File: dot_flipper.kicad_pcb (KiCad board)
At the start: 2 copper layers, 71 x 10 mm, 3 parts, among them U1 7_flip_dots

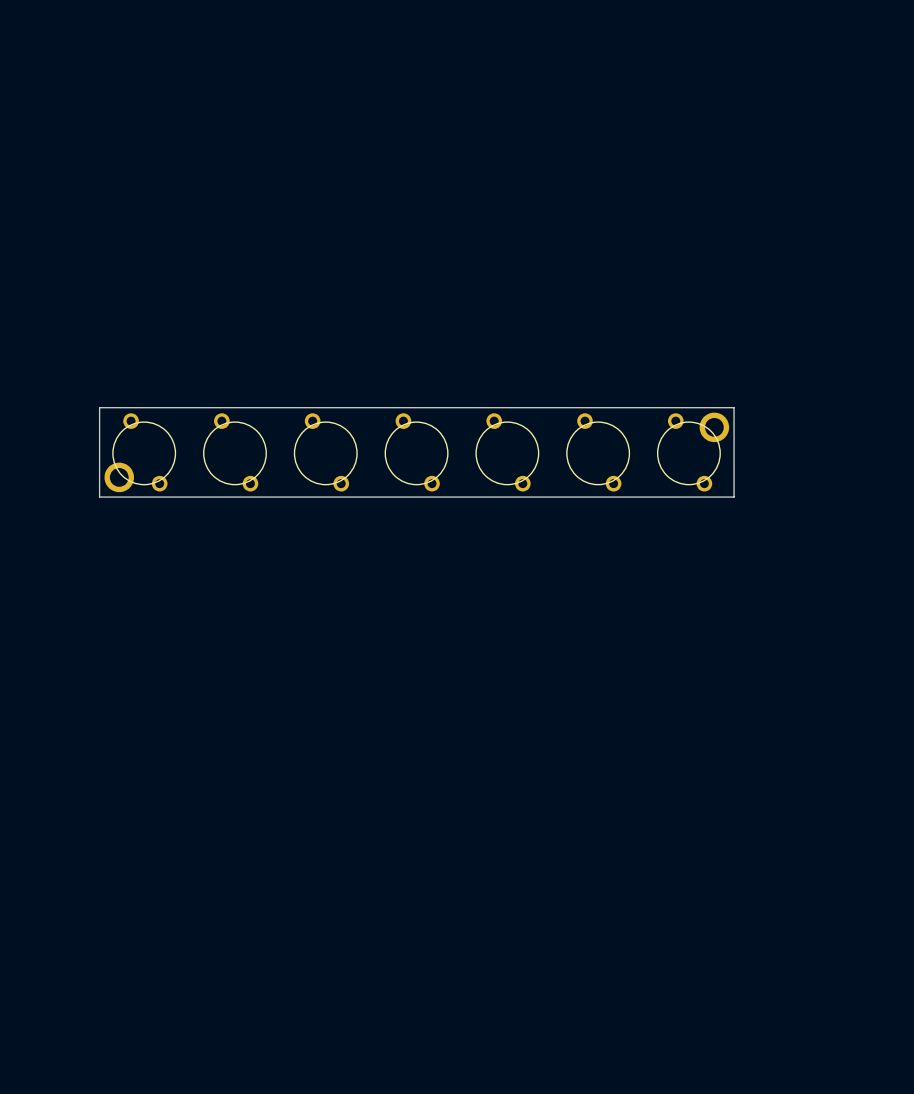
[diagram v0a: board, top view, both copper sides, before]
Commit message: Rough component placement
Slightly tweaked flipdot footprint to match my measurements and datasheet better
Created board outline, interfaces.
Rough component placement.
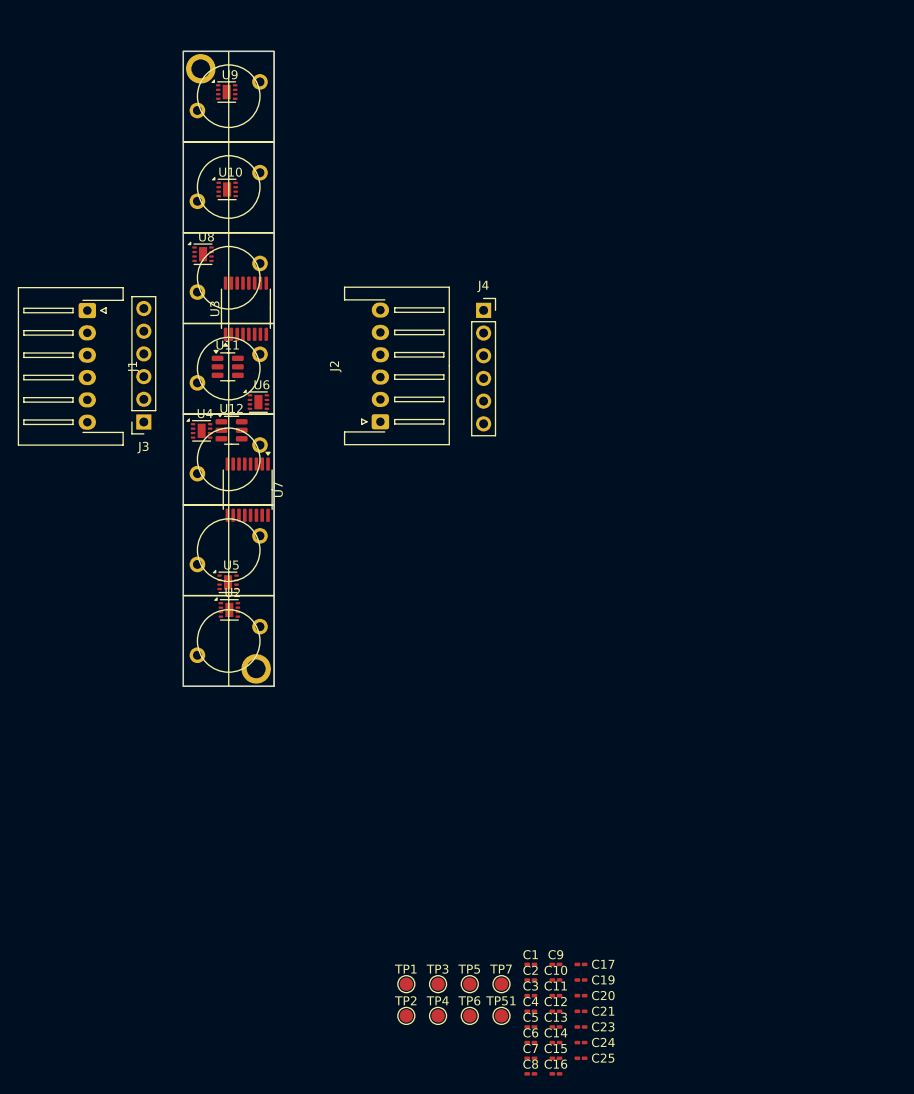
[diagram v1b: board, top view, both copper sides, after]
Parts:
- added C1: 100n/16V, Capacitor_SMD:C_0201_0603Metric_Pad0.64x0.40mm_HandSolder, F.Cu at (80.8, 122.1)
- added C10: 100n/16V, Capacitor_SMD:C_0201_0603Metric_Pad0.64x0.40mm_HandSolder, F.Cu at (83.7, 123.8)
- added C11: 100n/16V, Capacitor_SMD:C_0201_0603Metric_Pad0.64x0.40mm_HandSolder, F.Cu at (83.7, 125.6)
- added C12: 10uF/16V, Capacitor_SMD:C_0201_0603Metric_Pad0.64x0.40mm_HandSolder, F.Cu at (83.7, 127.3)
- added C13: 10uF/16V, Capacitor_SMD:C_0201_0603Metric_Pad0.64x0.40mm_HandSolder, F.Cu at (83.7, 129.1)
- added C14: 100n, Capacitor_SMD:C_0201_0603Metric_Pad0.64x0.40mm_HandSolder, F.Cu at (83.7, 130.8)
- added C15: 100n/16V, Capacitor_SMD:C_0201_0603Metric_Pad0.64x0.40mm_HandSolder, F.Cu at (83.7, 132.6)
- added C16: 100n/16V, Capacitor_SMD:C_0201_0603Metric_Pad0.64x0.40mm_HandSolder, F.Cu at (83.7, 134.3)
- added C17: 100n/16V, Capacitor_SMD:C_0201_0603Metric_Pad0.64x0.40mm_HandSolder, F.Cu at (86.5, 122.1)
- added C19: 100n/16V, Capacitor_SMD:C_0201_0603Metric_Pad0.64x0.40mm_HandSolder, F.Cu at (86.5, 123.8)
- added C2: 100n/16V, Capacitor_SMD:C_0201_0603Metric_Pad0.64x0.40mm_HandSolder, F.Cu at (80.8, 123.8)
- added C20: 100n/16V, Capacitor_SMD:C_0201_0603Metric_Pad0.64x0.40mm_HandSolder, F.Cu at (86.5, 125.6)
- added C21: 100n/16V, Capacitor_SMD:C_0201_0603Metric_Pad0.64x0.40mm_HandSolder, F.Cu at (86.5, 127.3)
- added C23: 10uF/16V, Capacitor_SMD:C_0201_0603Metric_Pad0.64x0.40mm_HandSolder, F.Cu at (86.5, 129.1)
- added C24: 10uF/16V, Capacitor_SMD:C_0201_0603Metric_Pad0.64x0.40mm_HandSolder, F.Cu at (86.5, 130.8)
- added C25: 10uF/16V, Capacitor_SMD:C_0201_0603Metric_Pad0.64x0.40mm_HandSolder, F.Cu at (86.5, 132.6)
- added C3: 100n, Capacitor_SMD:C_0201_0603Metric_Pad0.64x0.40mm_HandSolder, F.Cu at (80.8, 125.6)
- added C4: 10uF/16V, Capacitor_SMD:C_0201_0603Metric_Pad0.64x0.40mm_HandSolder, F.Cu at (80.8, 127.3)
- added C5: 100n/16V, Capacitor_SMD:C_0201_0603Metric_Pad0.64x0.40mm_HandSolder, F.Cu at (80.8, 129.1)
- added C6: 100n/16V, Capacitor_SMD:C_0201_0603Metric_Pad0.64x0.40mm_HandSolder, F.Cu at (80.8, 130.8)
- added C7: 10uF/16V, Capacitor_SMD:C_0201_0603Metric_Pad0.64x0.40mm_HandSolder, F.Cu at (80.8, 132.6)
- added C8: 100n/16V, Capacitor_SMD:C_0201_0603Metric_Pad0.64x0.40mm_HandSolder, F.Cu at (80.8, 134.3)
- added C9: 100n/16V, Capacitor_SMD:C_0201_0603Metric_Pad0.64x0.40mm_HandSolder, F.Cu at (83.7, 122.1)
- added J1: Conn_01x06_Socket, Connector_JST:JST_XH_S6B-XH-A-1_1x06_P2.50mm_Horizontal, F.Cu at (31.2, 48.9)
- added J2: Conn_01x06_Socket, Connector_JST:JST_XH_S6B-XH-A-1_1x06_P2.50mm_Horizontal, F.Cu at (64.0, 61.3)
- added J3: Conn_01x06_Socket, Connector_PinSocket_2.54mm:PinSocket_1x06_P2.54mm_Vertical, F.Cu at (37.5, 61.4)
- added J4: Conn_01x06_Socket, Connector_PinSocket_2.54mm:PinSocket_1x06_P2.54mm_Vertical, F.Cu at (75.6, 48.9)
- added TP1: SEROUT1, TestPoint:TestPoint_Pad_D1.5mm, F.Cu at (66.9, 124.3)
- added TP2: SLEEP, TestPoint:TestPoint_Pad_D1.5mm, F.Cu at (66.9, 127.8)
- added TP3: LATCH, TestPoint:TestPoint_Pad_D1.5mm, F.Cu at (70.5, 124.3)
- added TP4: SRCLK, TestPoint:TestPoint_Pad_D1.5mm, F.Cu at (70.5, 127.8)
- added TP5: SERIN, TestPoint:TestPoint_Pad_D1.5mm, F.Cu at (74.0, 124.3)
- added TP51: SEROUT2, TestPoint:TestPoint_Pad_D1.5mm, F.Cu at (77.6, 127.8)
- added TP6: VCC, TestPoint:TestPoint_Pad_D1.5mm, F.Cu at (74.0, 127.8)
- added TP7: GND, TestPoint:TestPoint_Pad_D1.5mm, F.Cu at (77.6, 124.3)
- added U10: DRV8837C, Package_SON:WSON-8-1EP_2x2mm_P0.5mm_EP0.9x1.6mm, F.Cu at (46.9, 35.3)
- added U11: CDSOT236-T05C, Package_TO_SOT_SMD:SOT-23-6, F.Cu at (46.9, 55.2)
- added U12: CDSOT236-T05C, Package_TO_SOT_SMD:SOT-23-6, F.Cu at (47.4, 62.3)
- added U2: DRV8837C, Package_SON:WSON-8-1EP_2x2mm_P0.5mm_EP0.9x1.6mm, F.Cu at (47.1, 82.4)
- added U3: 74HC595, Package_SO:TSSOP-16_4.4x5mm_P0.65mm, F.Cu at (49.0, 48.7)
- added U4: DRV8837C, Package_SON:WSON-8-1EP_2x2mm_P0.5mm_EP0.9x1.6mm, F.Cu at (44.0, 62.4)
- added U5: DRV8837C, Package_SON:WSON-8-1EP_2x2mm_P0.5mm_EP0.9x1.6mm, F.Cu at (47.0, 79.3)
- added U6: DRV8837C, Package_SON:WSON-8-1EP_2x2mm_P0.5mm_EP0.9x1.6mm, F.Cu at (50.4, 59.1)
- added U7: 74HC595, Package_SO:TSSOP-16_4.4x5mm_P0.65mm, F.Cu at (49.2, 68.9)
- added U8: DRV8837C, Package_SON:WSON-8-1EP_2x2mm_P0.5mm_EP0.9x1.6mm, F.Cu at (44.2, 42.6)
- added U9: DRV8837C, Package_SON:WSON-8-1EP_2x2mm_P0.5mm_EP0.9x1.6mm, F.Cu at (46.8, 24.4)
- moved H2 70.1 mm to (43.9, 21.8)
- moved U1 27.2 mm to (43.5, 87.5), turned to 90 degrees
- moved H1 26.3 mm to (50.1, 89.0)
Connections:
- U1 pad 1-UA: unconnected-(U1A-a-Pad1-UA) -> Net-(U1A-a)
- U1 pad 1-UB: unconnected-(U1B-a-Pad1-UB) -> Net-(U1B-a)
- U1 pad 1-UC: unconnected-(U1C-a-Pad1-UC) -> Net-(U1C-a)
- U1 pad 1-UD: unconnected-(U1D-a-Pad1-UD) -> Net-(U1D-a)
- U1 pad 1-UE: unconnected-(U1E-a-Pad1-UE) -> Net-(U1E-a)
- U1 pad 1-UF: unconnected-(U1F-a-Pad1-UF) -> Net-(U10-OUT2)
- U1 pad 1-UG: unconnected-(U1G-a-Pad1-UG) -> Net-(U1G-a)
- U1 pad 2-UA: unconnected-(U1A-b-Pad2-UA) -> Net-(U1A-b)
- U1 pad 2-UB: unconnected-(U1B-b-Pad2-UB) -> Net-(U1B-b)
- U1 pad 2-UC: unconnected-(U1C-b-Pad2-UC) -> Net-(U1C-b)
- U1 pad 2-UD: unconnected-(U1D-b-Pad2-UD) -> Net-(U1D-b)
- U1 pad 2-UE: unconnected-(U1E-b-Pad2-UE) -> Net-(U1E-b)
- U1 pad 2-UF: unconnected-(U1F-b-Pad2-UF) -> Net-(U10-OUT1)
- U1 pad 2-UG: unconnected-(U1G-b-Pad2-UG) -> Net-(U1G-b)
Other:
- board size 71 x 10 mm -> 10.2 x 71 mm
- board text removed: "+"
- board text removed: "-"
- board text removed: ".wordpress.com"
- board text removed: "12V"
- board text removed: "C"
- board text removed: "CLK"
- board text removed: "D"
- board text removed: "DATA"
- board text removed: "DOT FLIPPER v1.1"
- board text removed: "GND"
- board text removed: "INPUT"
- board text removed: "OPT1"
- board text removed: "OPT2"
- board text removed: "OUTPUT"
- board text removed: "P"
- board text removed: "PierreMuth"

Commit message: Power supply mod
Connected VM to VCC to simplify operation and make PCB layout easier
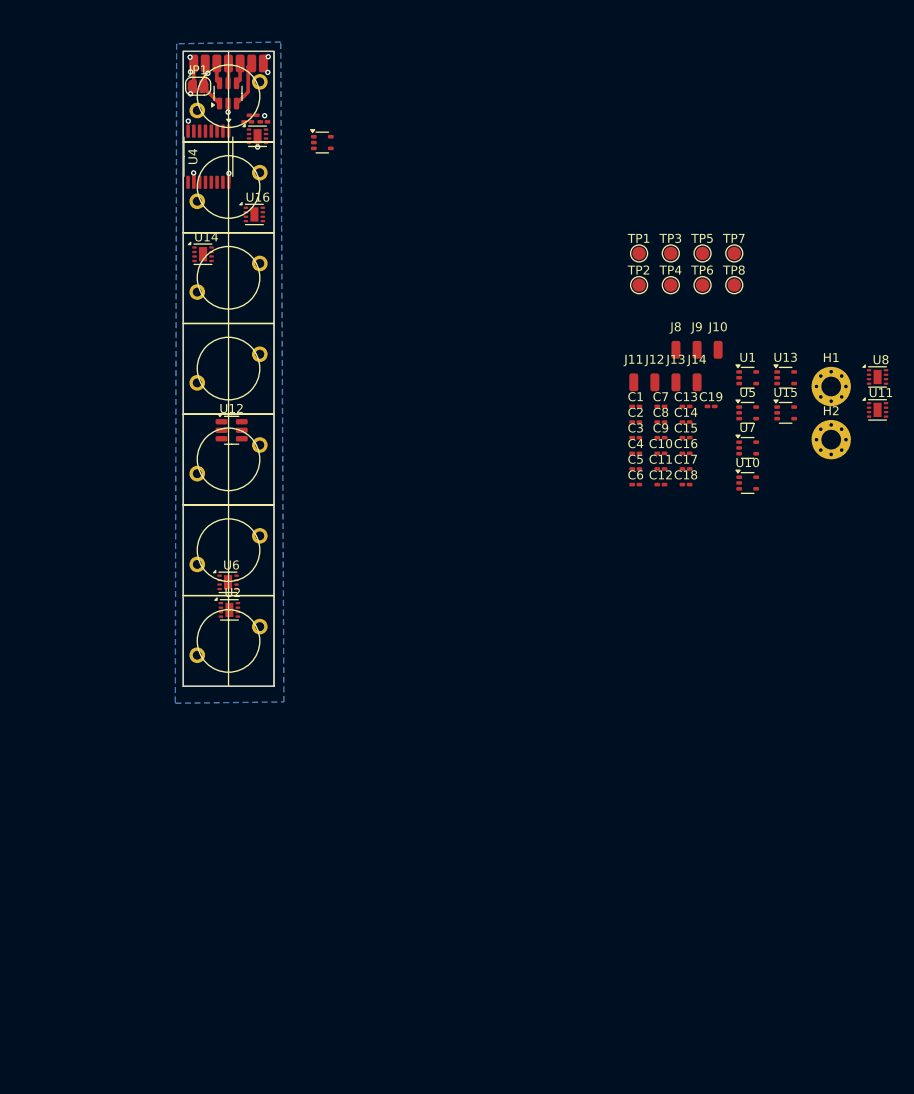
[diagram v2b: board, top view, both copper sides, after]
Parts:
- removed C23, C24, C25: 10uF/16V, Capacitor_SMD:C_0201_0603Metric_Pad0.64x0.40mm_HandSolder
- removed TP51: SEROUT2, TestPoint:TestPoint_Pad_D1.5mm
- removed the U3 at (49.0, 48.7)
- removed the U6 at (50.4, 59.1)
- added C18: 100n/16V, Capacitor_SMD:C_0201_0603Metric_Pad0.64x0.40mm_HandSolder, F.Cu at (98.2, 68.4)
- added C22: 10uF/16V, Capacitor_SMD:C_0201_0603Metric_Pad0.64x0.40mm_HandSolder, F.Cu at (49.8, 27.0)
- added J10: SEROUT, Connector_Wire:SolderWirePad_1x01_SMD_1x2mm, F.Cu at (101.8, 53.3)
- added J11: SRCLK_o, Connector_Wire:SolderWirePad_1x01_SMD_1x2mm, F.Cu at (92.4, 56.9)
- added J12: LATCH_o, Connector_Wire:SolderWirePad_1x01_SMD_1x2mm, F.Cu at (94.7, 56.9)
- added J13: SLEEP_o, Connector_Wire:SolderWirePad_1x01_SMD_1x2mm, F.Cu at (97.1, 56.9)
- added J14: GND_o, Connector_Wire:SolderWirePad_1x01_SMD_1x2mm, F.Cu at (99.4, 56.9)
- added J5: LATCH_i, Connector_Wire:SolderWirePad_1x01_SMD_1x2mm, F.Cu at (48.3, 21.2)
- added J6: SLEEP_i, Connector_Wire:SolderWirePad_1x01_SMD_1x2mm, F.Cu at (49.6, 21.2)
- added J7: GND_i, Connector_Wire:SolderWirePad_1x01_SMD_1x2mm, F.Cu at (50.9, 21.2)
- added J8: VM_o, Connector_Wire:SolderWirePad_1x01_SMD_1x2mm, F.Cu at (97.1, 53.3)
- added J9: VCC_o, Connector_Wire:SolderWirePad_1x01_SMD_1x2mm, F.Cu at (99.4, 53.3)
- added JP1: SolderJumper_2_Open, Jumper:SolderJumper-2_P1.3mm_Open_RoundedPad1.0x1.5mm, F.Cu at (43.6, 23.8)
- added TP8: GND, TestPoint:TestPoint_Pad_D1.5mm, F.Cu at (103.6, 46.1)
- added U1: SN74LVC1G04DCKR, Package_TO_SOT_SMD:SOT-353_SC-70-5, F.Cu at (105.1, 56.4)
- added U10: SN74LVC1G04DCKR, Package_TO_SOT_SMD:SOT-353_SC-70-5, F.Cu at (105.1, 68.2)
- added U11: DRV8837CDSGR, Package_SON:WSON-8-1EP_2x2mm_P0.5mm_EP0.9x1.6mm, F.Cu at (119.6, 60.0)
- added U13: SN74LVC1G04DCKR, Package_TO_SOT_SMD:SOT-353_SC-70-5, F.Cu at (109.4, 56.4)
- added U15: SN74LVC1G04DCKR, Package_TO_SOT_SMD:SOT-353_SC-70-5, F.Cu at (109.4, 60.3)
- added U17: SN74LVC1G04DCKR, Package_TO_SOT_SMD:SOT-353_SC-70-5, F.Cu at (57.5, 30.1)
- added U5: SN74LVC1G04DCKR, Package_TO_SOT_SMD:SOT-353_SC-70-5, F.Cu at (105.1, 60.3)
- added U8: DRV8837CDSGR, Package_SON:WSON-8-1EP_2x2mm_P0.5mm_EP0.9x1.6mm, F.Cu at (119.6, 56.3)
- C10, C16, C19: value 100n/16V -> 10uF/16V
- C12: value 10uF/16V -> 100n/16V
- C14: value 100n -> 100n/16V
- C3: value 100n -> 10uF/16V
- C4: value 10uF/16V -> 100n
- H1, H2: footprint dot_flipper:MountingHole_2.2mm_M2_Pad_thin -> MountingHole:MountingHole_2.2mm_M2_Pad_Via
- J1: value Conn_01x06_Socket -> VM_i; footprint Connector_JST:JST_XH_S6B-XH-A-1_1x06_P2.50mm_Horizontal -> Connector_Wire:SolderWirePad_1x01_SMD_1x2mm
- J2: value Conn_01x06_Socket -> VCC_i; footprint Connector_JST:JST_XH_S6B-XH-A-1_1x06_P2.50mm_Horizontal -> Connector_Wire:SolderWirePad_1x01_SMD_1x2mm
- J3: value Conn_01x06_Socket -> SERIN; footprint Connector_PinSocket_2.54mm:PinSocket_1x06_P2.54mm_Vertical -> Connector_Wire:SolderWirePad_1x01_SMD_1x2mm
- J4: value Conn_01x06_Socket -> SRCLK_i; footprint Connector_PinSocket_2.54mm:PinSocket_1x06_P2.54mm_Vertical -> Connector_Wire:SolderWirePad_1x01_SMD_1x2mm
- TP1: value SEROUT1 -> SEROUT
- TP2: value SLEEP -> SRCLK
- TP4: value SRCLK -> SLEEP
- U14: renamed from U8; value DRV8837C -> DRV8837CDSGR
- U16: renamed from U10; value DRV8837C -> DRV8837CDSGR
- U18: renamed from U9; value DRV8837C -> DRV8837CDSGR
- U2: value DRV8837C -> DRV8837CDSGR
- U4: value DRV8837C -> SN74HC595PWR; footprint Package_SON:WSON-8-1EP_2x2mm_P0.5mm_EP0.9x1.6mm -> Package_SO:TSSOP-16_4.4x5mm_P0.65mm
- U6: renamed from U5; value DRV8837C -> DRV8837CDSGR
- U7: value 74HC595 -> SN74LVC1G04DCKR; footprint Package_SO:TSSOP-16_4.4x5mm_P0.65mm -> Package_TO_SOT_SMD:SOT-353_SC-70-5
- moved C21 106.3 mm to (49.2, 27.8)
- moved C20 104.0 mm to (51.0, 27.8), turned to 180 degrees
- moved TP1 85.8 mm to (93.0, 42.5)
- moved TP2 85.8 mm to (93.0, 46.1)
- moved TP3 85.8 mm to (96.5, 42.5)
- moved TP4 85.8 mm to (96.5, 46.1)
- moved TP5 85.8 mm to (100.1, 42.5)
- moved TP6 85.8 mm to (100.1, 46.1)
- moved TP7 85.8 mm to (103.6, 42.5)
- moved H2 81.9 mm to (114.5, 63.3)
- moved C7 74.4 mm to (95.4, 59.6)
- moved C8 74.4 mm to (95.4, 61.4)
- moved H1 71.7 mm to (114.5, 57.4)
- moved C13 71.0 mm to (98.2, 59.6)
- moved C14 71.0 mm to (98.2, 61.4)
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- renumbered U1 to U3, U11 to U9
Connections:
- C11 pad 1: VM -> VCC
- C15 pad 1: VCC -> VM
- C16 pad 1: VCC -> VM
- C20 pad 1: VM -> VCC
- C3 pad 1: VCC -> VM
- C4 pad 1: VM -> VCC
- C9 pad 1: VCC -> VM
- J1 pad 1: VCC -> VM
- J3 pad 1: GND -> /SERIN
- J4 pad 1: GND -> /SRCLK
- TP1 pad 1: /SEROUT1 -> /SEROUT
- TP2 pad 1: /SLEEP -> /SRCLK
- TP4 pad 1: /SRCLK -> /SLEEP
- U12 pad 1: /SEROUT2 -> /SEROUT
- U14 pad 5: Net-(U7-QB) -> /OUT5
- U14 pad 6: Net-(U7-QA) -> Net-(U14-IN1)
- U16 pad 5: Net-(U10-IN2) -> /OUT6
- U16 pad 6: Net-(U10-IN1) -> Net-(U16-IN1)
- U18 pad 5: Net-(U7-QF) -> /OUT7
- U18 pad 6: Net-(U7-QE) -> Net-(U18-IN1)
- U2 pad 5: Net-(U2-IN2) -> /OUT1
- U3 pad 1-UC: Net-(U1C-a) -> Net-(U3C-a)
- U3 pad 2-UC: Net-(U1C-b) -> Net-(U3C-b)
- U4 pad 1: VM -> /OUT2
- U4 pad 2: Net-(U1C-b) -> /OUT3
- U4 pad 3: Net-(U1C-a) -> /OUT4
- U4 pad 4: GND -> /OUT5
- U4 pad 5: Net-(U3-QF) -> /OUT6
- U4 pad 6: Net-(U3-QE) -> /OUT7
- U4 pad 7: /SLEEP -> unconnected-(U4-QH-Pad7)
- U4 pad 8: VCC -> GND
- U4 pad 9: GND -> /SEROUT
- U6 pad 5: Net-(U3-QD) -> /OUT2
- U7 pad 1: Net-(U7-QB) -> unconnected-(U7-NC-Pad1)
- U7 pad 2: Net-(U10-IN1) -> /OUT3
- U7 pad 3: Net-(U10-IN2) -> GND
- U7 pad 4: Net-(U7-QE) -> Net-(U8-IN1)
- U7 pad 5: Net-(U7-QF) -> VCC
- U9 pad 1: /SERIN -> VCC
- U9 pad 3: /SRCLK -> /SLEEP
- U9 pad 5: VCC -> /SRCLK
- U9 pad 6: /SLEEP -> /SERIN
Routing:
- net VCC: track 0.00 -> 8.57 mm, vias 0 -> 4
- net VM: track 0.00 -> 5.52 mm, vias 0 -> 3
- net /SLEEP: track 0.00 -> 5.19 mm
- net GND: track 0.00 -> 4.35 mm, vias 0 -> 5
- net /LATCH: track 0.00 -> 2.38 mm
- net /SERIN: track 0.00 -> 2.34 mm
- net /SRCLK: track 0.00 -> 2.23 mm
- added copper zone on B.Cu, net GND
- added copper zone on In2.Cu, net VCC
- added copper zone on In1.Cu, net VM
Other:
- copper layers 2 -> 4
